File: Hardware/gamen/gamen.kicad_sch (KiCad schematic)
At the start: 68 parts, among them J1 POWER IN, J2 Conn_01x05_Pin, J3 UART_Header, J4 MIDI CONN, J5 SCREEN CONN, SW1 SW_SPDT, U1 TPS562201DDCR, U2 STM32H743IITx, U3 AS4C16M16SA-6TIN, U4 W25Q256JWPIQ, U7 TLP2361(E, Y1 25MHz

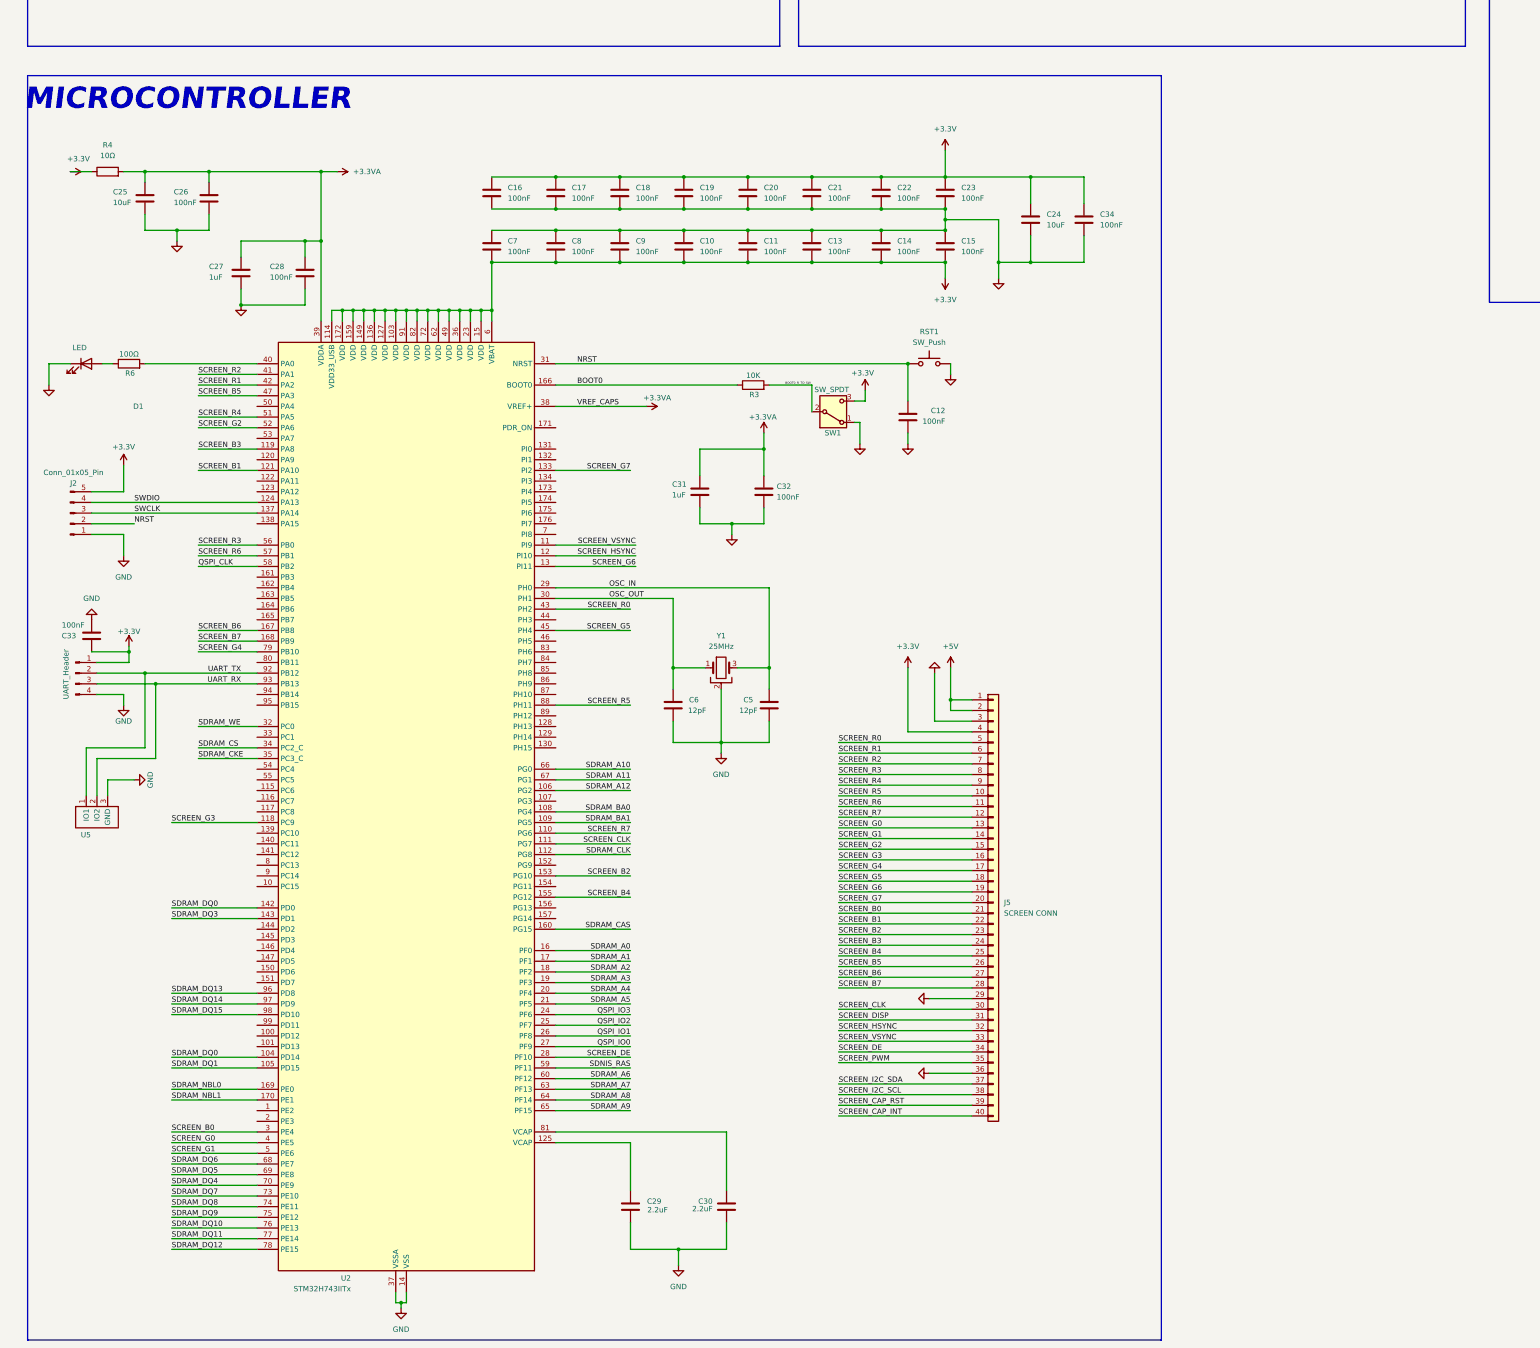
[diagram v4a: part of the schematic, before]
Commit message: Remvoed 3.3V on shori UART and changed tantalum cap
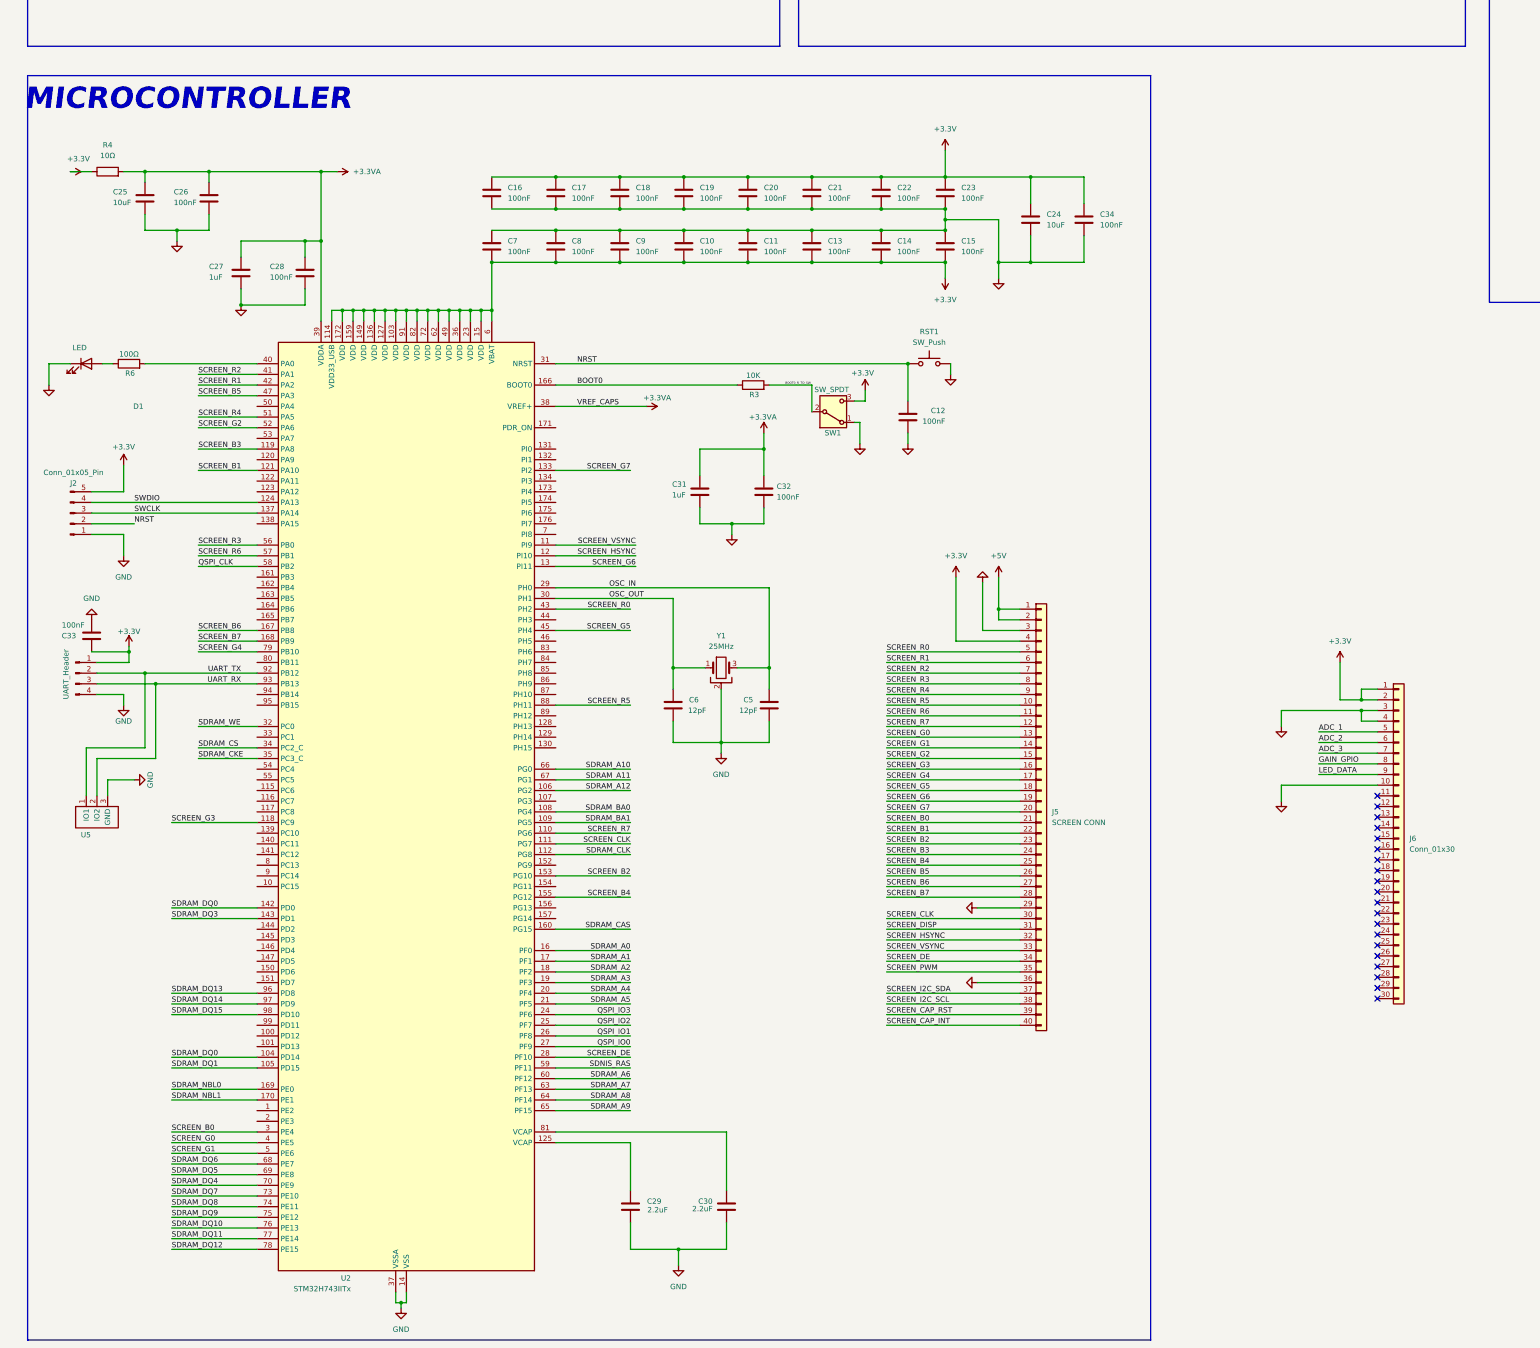
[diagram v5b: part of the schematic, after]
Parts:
- added J6: Conn_01x30, symbol Connector_Generic:Conn_01x30
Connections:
- net +3.3V: now also J6.1 (Pin_1), J6.2 (Pin_2)
- net GND: now also J6.10 (Pin_10), J6.3 (Pin_3), J6.4 (Pin_4)
- new net ADC_1: J6.5 (Pin_5)
- new net ADC_2: J6.6 (Pin_6)
- new net ADC_3: J6.7 (Pin_7)
- new net GAIN_GPIO: J6.8 (Pin_8)
- new net LED_DATA: J6.9 (Pin_9)
- no-connect marks 1 -> 21
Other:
- moved on the sheet: J5
